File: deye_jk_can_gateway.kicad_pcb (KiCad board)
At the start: 4 copper layers, 45 x 62 mm, 77 parts, among them J1 R-RJ45R08P-B000, J2 Pinheader 1x4 2.54mm, J3 XH-4A, J5 Pinheader 1x4 2.54mm, J6 TYPE-C16PIN, J7 Conn_01x06_Pin, SW1 TPS645-5NC105, SW2 TPS645-5NC105, U1 ESP32-S2-MINI-2U-N4R2, U2 TJA1042T-3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

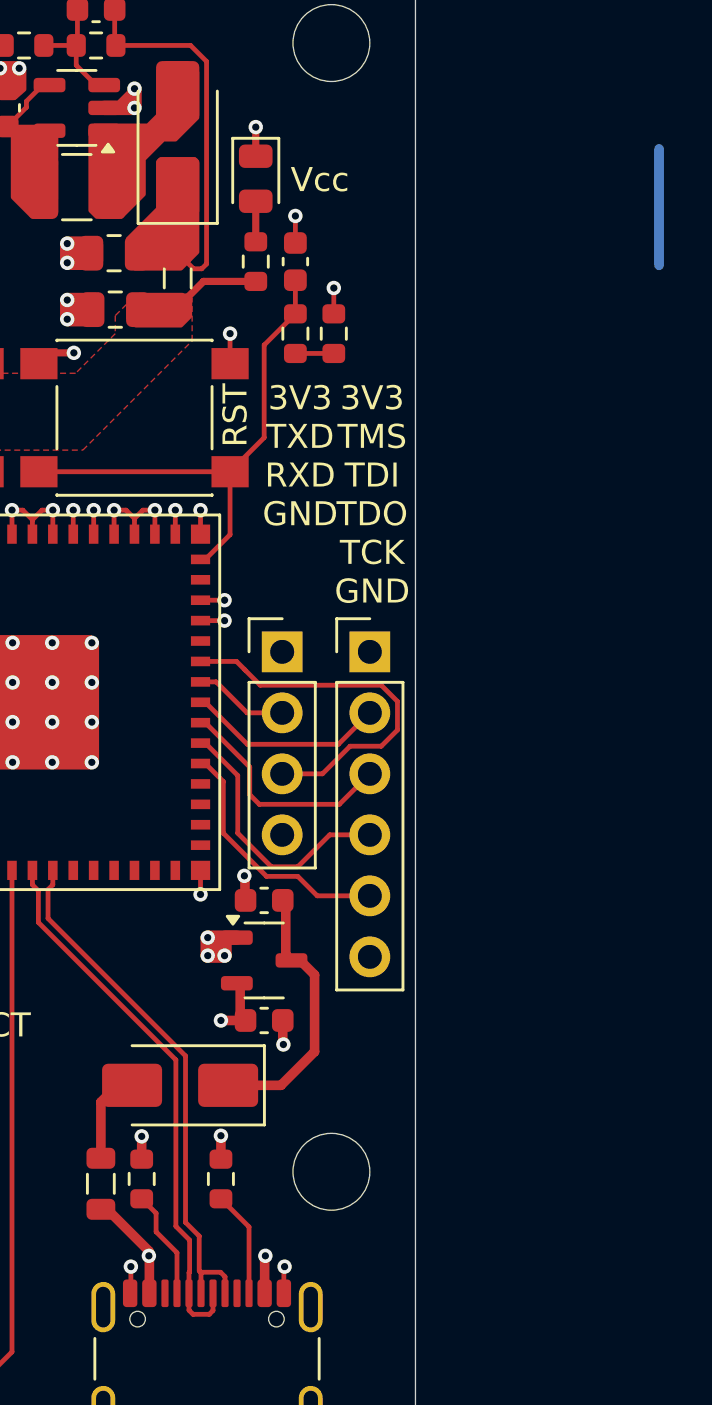
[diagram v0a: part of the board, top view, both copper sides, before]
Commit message: filled ground plane
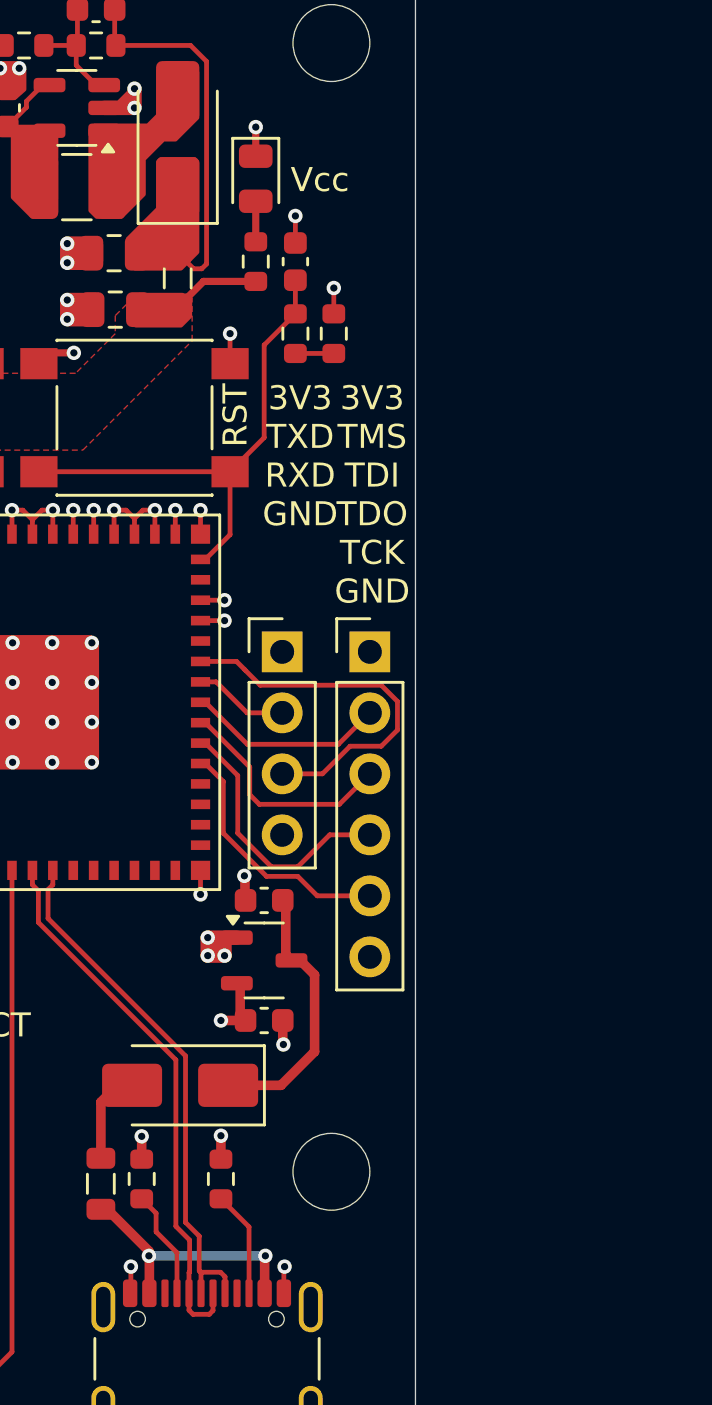
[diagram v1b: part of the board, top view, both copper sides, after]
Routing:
- net GND: track 81.0 -> 78.0 mm
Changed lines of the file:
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@@
-	)
-	(segment
-		(start 133.16 116.8)
-		(end 132.21 115.85)
-		(width 0.3)
-		(layer "In1.Cu")
-		(net 2)
-	)
-	(segment
-		(start 133.16 116.8)
-		(end 133.15 116.8)
-		(width 0.3)
-		(layer "In1.Cu")
-		(net 2)
-	)
-	(segment
-		(start 132.21 115.85)
-		(end 132.2 115.85)
-		(width 0.3)
-		(layer "In1.Cu")
-		(net 2)
-	)
-	(segment
-		(start 133.15 116.8)
-		(end 132 117.95)
-		(width 0.3)
-		(layer "In1.Cu")
-		(net 2)
 	)
 	(segment
@@
 	)
 	(segment
-		(start 134.15 98.75)
-		(end 134.15 93.9)
+		(start 112.907107 139.992893)
+		(end 117.757107 139.992893)
 		(width 0.4)
 		(layer "B.Cu")
@@
 		(min_thickness 0.2)
 		(filled_areas_thickness no)
-		(fill
+		(fill yes
 			(thermal_gap 0.4)
 			(thermal_bridge_width 0.3)
@@
 		(min_thickness 0.2)
 		(filled_areas_thickness no)
-		(fill
+		(fill yes
 			(thermal_gap 0.4)
 			(thermal_bridge_width 0.3)
